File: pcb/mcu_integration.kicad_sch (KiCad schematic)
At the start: 39 parts, among them J5 DM3BT-DSF-PEJS, U1 STM32F103RBTx, U2 LMT87DCKT, U8 LTC4300A-1IMS8_PBF, Y1 ECS-80-18-5PX-GM-TR

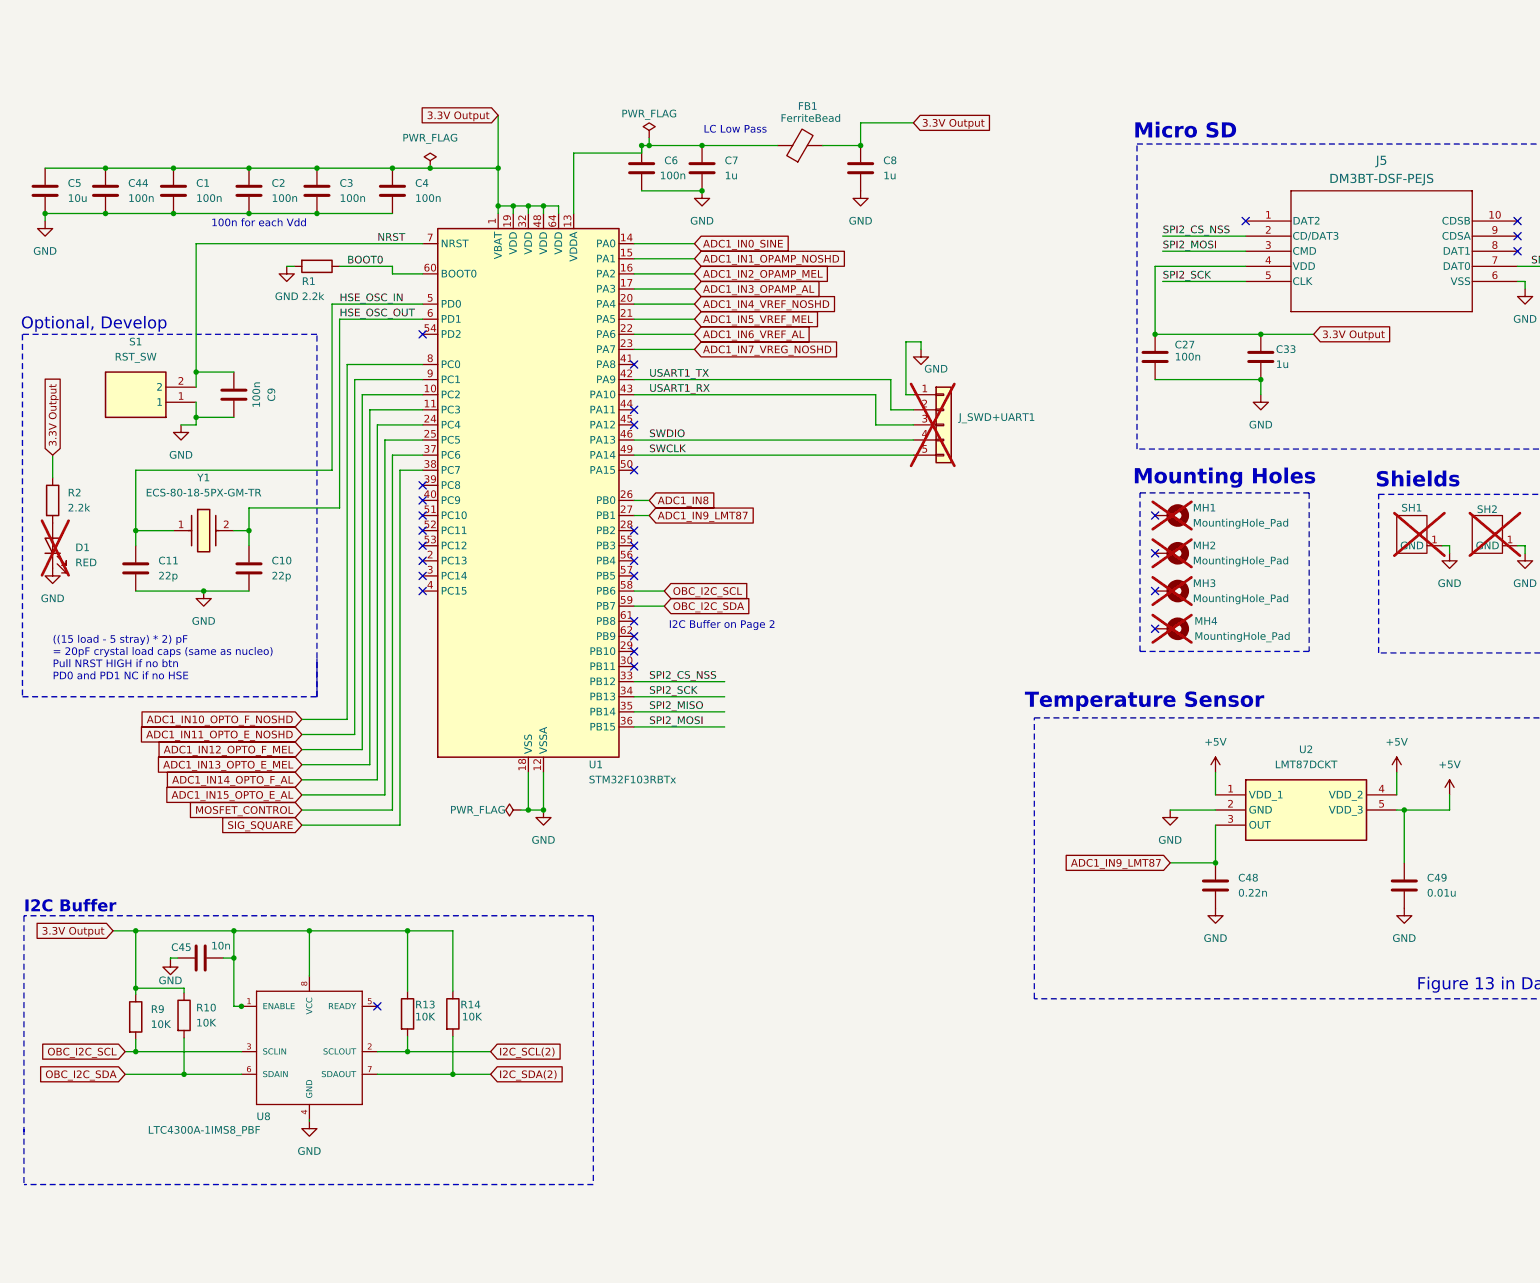
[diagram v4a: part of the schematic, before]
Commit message: updated schematic lables
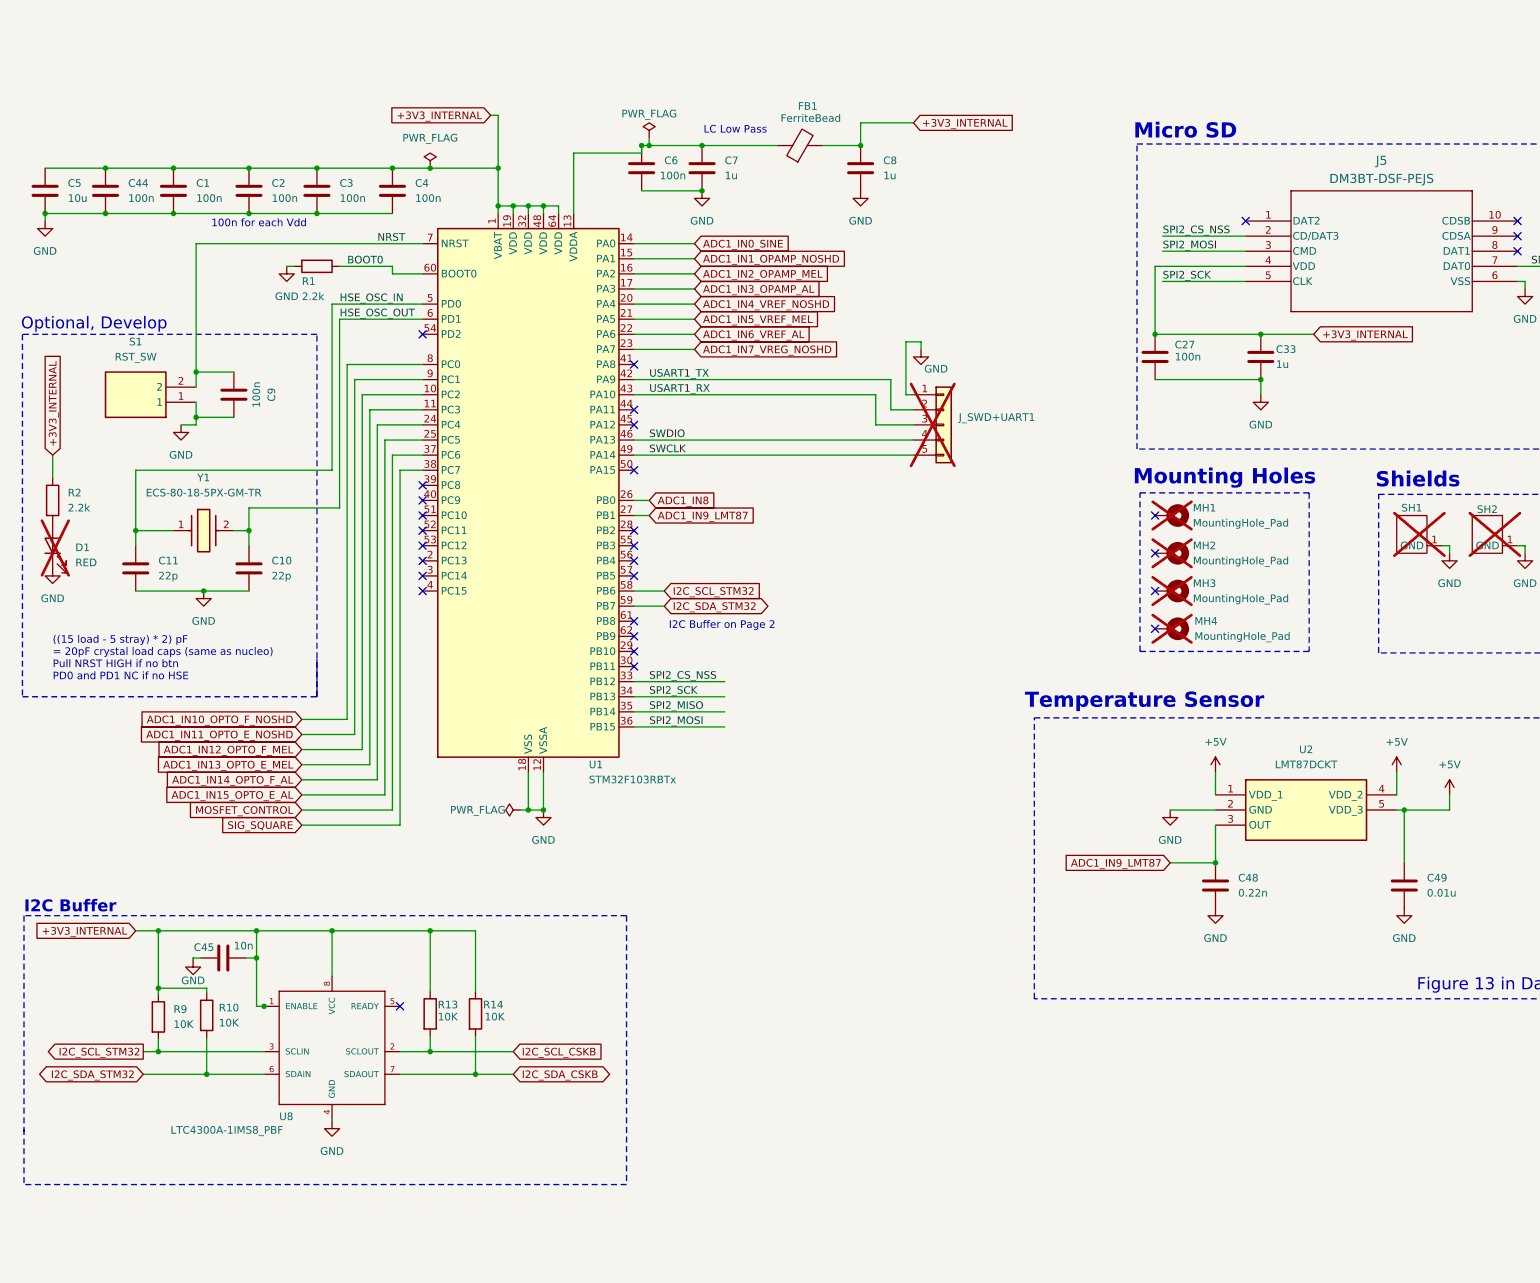
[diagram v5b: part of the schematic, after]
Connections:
- net 3.3V Output renamed +3V3_INTERNAL
- net I2C_SCL(2) renamed I2C_SCL_CSKB
- net I2C_SDA(2) renamed I2C_SDA_CSKB
- net OBC_I2C_SCL renamed I2C_SCL_STM32
- net OBC_I2C_SDA renamed I2C_SDA_STM32
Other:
- moved on the sheet: C45, R10, R13, R14, R9, U8

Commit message: Changed spacing of test ICs to allow for larger melanin domes
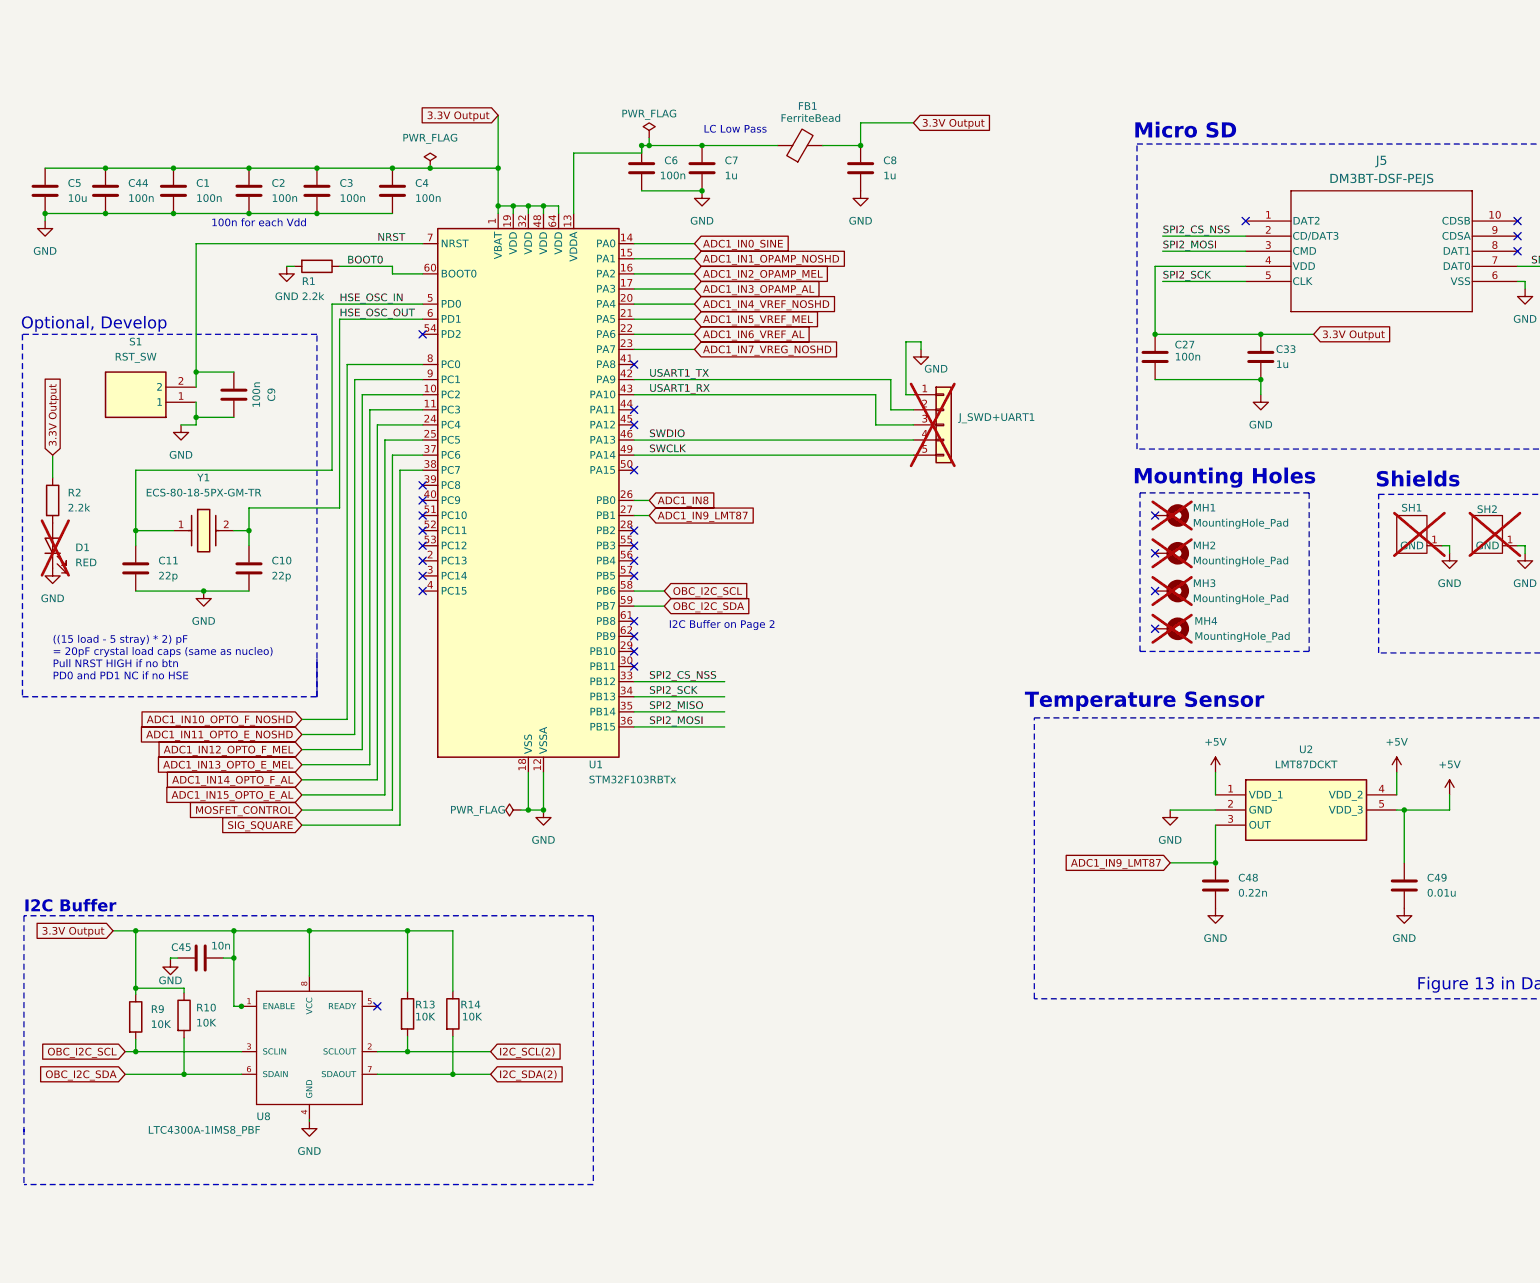
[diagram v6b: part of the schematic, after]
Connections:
- net +3V3_INTERNAL renamed 3.3V Output
- net I2C_SCL_CSKB renamed I2C_SCL(2)
- net I2C_SCL_STM32 renamed OBC_I2C_SCL
- net I2C_SDA_CSKB renamed I2C_SDA(2)
- net I2C_SDA_STM32 renamed OBC_I2C_SDA
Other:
- moved on the sheet: C45, R10, R13, R14, R9, U8

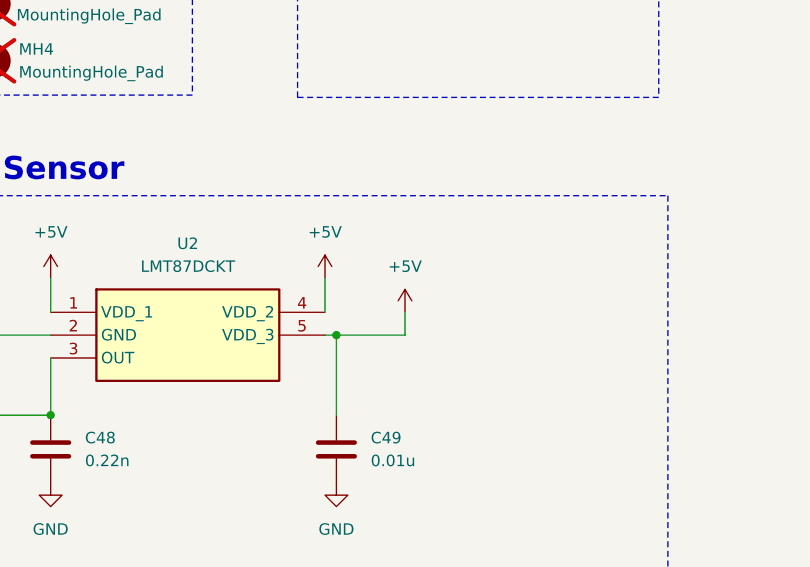
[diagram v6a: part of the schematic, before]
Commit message: Made minor changes for routing and decoup caps
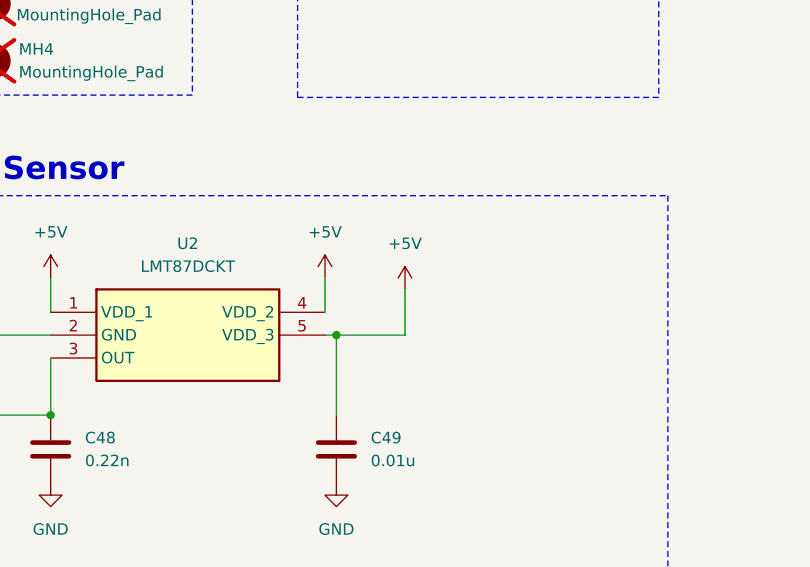
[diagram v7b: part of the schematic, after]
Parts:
- SH1, SH2, SH3: value ~ -> (none)

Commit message: Finished C25 BOM designation
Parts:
- C1, C2, C27, C3, C4, C44, C6, C9: Manufacturer_Part_Number GCM155R71C104KA55D -> (none)
- C10, C11: Manufacturer_Part_Number GCM1555C1H220JA16D -> (none)
- C33, C7, C8: Manufacturer_Part_Number GRT155R61C105KE01D -> (none)
- C45, C49: Manufacturer_Part_Number GCM155R71H103KA55D -> (none)
- C48: Manufacturer_Part_Number GCM1555C1H221JA16D -> (none)
- C5: Manufacturer_Part_Number GRT188R61C106KE13D -> (none)
- FB1: Manufacturer_Part_Number BLM18SG121TN1D -> (none)
- J5: Manufacturer_Part_Number DM3BT-DSF-PEJS -> (none)
- R1, R2: Manufacturer_Part_Number ERJ-2RKF2200X -> (none)
- R10, R13, R14, R9: Manufacturer_Part_Number ERJ-H2RF1002X -> (none)
- S1: Manufacturer_Part_Number 95C04A3GWRT -> (none)
- U1: Manufacturer_Part_Number STM32F103RBT7 -> (none)
- U2: Manufacturer_Part_Number LMT87DCKT -> (none)
- U8: MANUFACTURER_PART_NUMBER ltc4300a1ims8 -> (none); Manufacturer_Part_Number LTC4300A-1IMS8#PBF -> (none)
- Y1: Manufacturer_Part_Number ECS-80-18-5PX-GM-TR -> (none)
